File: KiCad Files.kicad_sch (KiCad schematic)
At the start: 2 parts

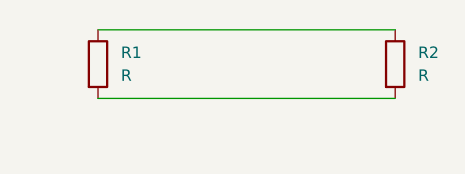
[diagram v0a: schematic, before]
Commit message: Fourth commit, included the custom schematic parts library to share as well
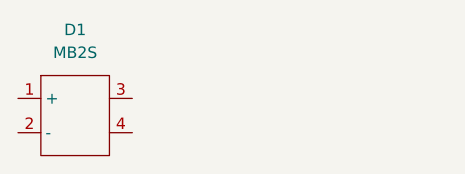
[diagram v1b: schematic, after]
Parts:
- removed R1, R2: R, symbol Device:R
- added D1: MB2S, symbol Custom_Symbols:MB2S
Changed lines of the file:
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@@
 	(generator_version "10.0")
 	(paper "A4")
-	(wire
-		(pts
-			(xy 134.62 92.71) (xy 167.64 92.71)
-		)
-		(stroke
-			(width 0)
-			(type default)
-		)
-	)
-	(wire
-		(pts
-			(xy 167.64 85.09) (xy 134.62 85.09)
-		)
-		(stroke
-			(width 0)
-			(type default)
-		)
-	)
 	(symbol
-		(lib_id "Device:R")
-		(at 134.62 88.9 0)
+		(lib_id "Custom_Symbols:MB2S")
+		(at 132.08 88.9 0)
 		(unit 1)
 		(body_style 1)
@@
 		(dnp no)
 		(fields_autoplaced yes)
-		(property "Reference" "R1"
-			(at 137.16 87.6299 0)
+		(property "Reference" "D1"
+			(at 132.08 85.09 0)
 			(show_name no)
 			(do_not_autoplace no)
@@
 					(size 1.27 1.27)
 				)
-				(justify left)
 			)
 		)
-		(property "Value" "R"
-			(at 137.16 90.1699 0)
+		(property "Value" "MB2S"
+			(at 132.08 87.63 0)
 			(show_name no)
 			(do_not_autoplace no)
@@
 					(size 1.27 1.27)
 				)
-				(justify left)
 			)
 		)
 		(property "Footprint" ""
-			(at 132.842 88.9 90)
+			(at 132.08 88.9 0)
 			(hide yes)
 			(show_name no)
@@
 			)
 		)
-		(property "Datasheet" ""
-			(at 134.62 88.9 0)
+		(property "Datasheet" "https://www.onsemi.com/pdf/datasheet/mb8s-d.pdf"
+			(at 132.08 88.9 0)
 			(hide yes)
 			(show_name no)
@@
 			)
 		)
-		(property "Description" "Resistor"
-			(at 134.62 88.9 0)
+		(property "Description" ""
+			(at 132.08 88.9 0)
 			(hide yes)
 			(show_name no)
@@
 			)
 		)
-		(pin "2"
+		(pin "4"
 		)
 		(pin "1"
+		)
+		(pin "3"
+		)
+		(pin "2"
 		)
 		(instances
 			(project "KiCad Files"
 				(path "/02e8e4b0-2d68-453f-9f10-22ddb8bef6dd"
-					(reference "R1")
+					(reference "D1")
 					(unit 1)
 				)
-			)
-		)
-	)
-	(symbol
-		(lib_id "Device:R")
-		(at 167.64 88.9 0)
-		(unit 1)
-		(body_style 1)
-		(exclude_from_sim no)
-		(in_bom yes)
-		(on_board yes)
-		(in_pos_files yes)
-		(dnp no)
-		(fields_autoplaced yes)
-		(property "Reference" "R2"
-			(at 170.18 87.6299 0)
-			(show_name no)
-			(do_not_autoplace no)
-			(effects
-				(font
-					(size 1.27 1.27)
-				)
-				(justify left)
-			)
-		)
-		(property "Value" "R"
-			(at 170.18 90.1699 0)
-			(show_name no)
-			(do_not_autoplace no)
-			(effects
-				(font
-					(size 1.27 1.27)
-				)
-				(justify left)
-			)
-		)
-		(property "Footprint" ""
-			(at 165.862 88.9 90)
-			(hide yes)
-			(show_name no)
-			(do_not_autoplace no)
-			(effects
-				(font
-					(size 1.27 1.27)
-				)
-			)
-		)
-		(property "Datasheet" ""
-			(at 167.64 88.9 0)
-			(hide yes)
-			(show_name no)
-			(do_not_autoplace no)
-			(effects
-				(font
-					(size 1.27 1.27)
-				)
-			)
-		)
-		(property "Description" "Resistor"
-			(at 167.64 88.9 0)
-			(hide yes)
-			(show_name no)
-			(do_not_autoplace no)
-			(effects
-				(font
-					(size 1.27 1.27)
-				)
-			)
-		)
-		(pin "2"
-		)
-		(pin "1"
-		)
-		(instances
-			(project "KiCad Files"
-				(path "/02e8e4b0-2d68-453f-9f10-22ddb8bef6dd"
-					(reference "R2")
-					(unit 1)
-				)
